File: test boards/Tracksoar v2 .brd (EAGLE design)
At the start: 50.4 x 19.6 mm, 53 parts, among them IC1 BME280, Y1 16MHZ

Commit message: added buck regulator
swapped the linear regulator for a buck converter.
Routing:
- net P$1: track 0.00 -> 9.58 mm, vias 0 -> 10
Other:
- board text added: "RX"
- board text added: "TX"
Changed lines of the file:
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@@
 <text x="-101.6" y="17.4752" size="0.6096" layer="25" rot="R270">3V</text>
 <text x="-99.695" y="17.4498" size="0.6096" layer="25" rot="R270">5V</text>
+<text x="-108.204" y="15.6718" size="0.8128" layer="25">RX</text>
+<text x="-108.077" y="17.8308" size="0.8128" layer="25">TX</text>
 </plain>
 <attributes>
@@
 <contactref element="C2" pad="1"/>
 <via x="-88.011" y="13.0048" extent="1-16" drill="0.5"/>
-<via x="-86.233" y="9.1186" extent="1-16" drill="0.5"/>
+<via x="-86.233" y="9.1186" extent="1-16" drill="0.6"/>
 <wire x1="-88.5444" y1="13.3604" x2="-88.1888" y2="13.0048" width="0.3048" layer="1"/>
 <wire x1="-88.1888" y1="13.0048" x2="-88.011" y2="13.0048" width="0.3048" layer="1"/>
@@
 <wire x1="-81.263" y1="11.2222" x2="-82.0212" y2="11.2222" width="0.3048" layer="16"/>
 <wire x1="-82.6262" y1="9.525" x2="-82.6516" y2="9.4996" width="0.3048" layer="16"/>
-<via x="-82.6516" y="9.4996" extent="1-16" drill="0.35"/>
+<via x="-82.6516" y="9.4996" extent="1-16" drill="0.6"/>
 <wire x1="-82.0212" y1="11.2222" x2="-82.6262" y2="10.6172" width="0.3048" layer="16"/>
 <wire x1="-82.6262" y1="10.6172" x2="-82.6262" y2="9.525" width="0.3048" layer="16"/>
@@
 <wire x1="-106.8832" y1="11.7498" x2="-107.5586" y2="11.7752" width="0.3048" layer="1"/>
 <wire x1="-107.5586" y1="11.7752" x2="-107.7824" y2="11.999" width="0.3048" layer="1"/>
-<via x="-108.7882" y="18.161" extent="1-16" drill="0.35" alwaysstop="yes"/>
+<via x="-108.7882" y="18.161" extent="1-16" drill="0.6" alwaysstop="yes"/>
 <wire x1="-111.6838" y1="18.1864" x2="-108.7882" y2="18.161" width="0.3048" layer="1"/>
 <wire x1="-112.5728" y1="17.2466" x2="-111.6838" y2="18.1864" width="0.3048" layer="1"/>
@@
 <wire x1="-109.6518" y1="17.4498" x2="-108.9152" y2="16.7132" width="0.3048" layer="1"/>
 <wire x1="-108.9152" y1="16.7132" x2="-108.9152" y2="16.129" width="0.3048" layer="1"/>
-<via x="-108.9152" y="16.129" extent="1-16" drill="0.35" alwaysstop="yes"/>
+<via x="-108.9152" y="16.129" extent="1-16" drill="0.6" alwaysstop="yes"/>
 <wire x1="-108.9152" y1="16.129" x2="-106.98" y2="14.1938" width="0.3048" layer="15"/>
 <wire x1="-104.729" y1="13.162" x2="-103.3018" y2="11.7348" width="0.3048" layer="15"/>
@@
 <wire x1="-106.98" y1="14.1938" x2="-105.23823125" y2="14.1938" width="0.3048" layer="15"/>
 <wire x1="-105.23823125" y1="14.1938" x2="-104.729" y2="13.68456875" width="0.3048" layer="15"/>
-<via x="-103.3018" y="11.7348" extent="1-16" drill="0.35"/>
+<via x="-103.3018" y="11.7348" extent="1-16" drill="0.6"/>
 <wire x1="-103.3018" y1="11.7348" x2="-103.3018" y2="11.1506" width="0.3048" layer="1"/>
 <wire x1="-103.3018" y1="11.1506" x2="-103.0732" y2="10.922" width="0.3048" layer="1"/>
@@
 <via x="-78.0034" y="4.064" extent="1-16" drill="1.183640625" diameter="1.6764" shape="square"/>
 </signal>
+<signal name="P$1">
+<via x="-79.2226" y="14.4018" extent="1-16" drill="0.35" alwaysstop="yes"/>
+<via x="-78.0034" y="14.4018" extent="1-16" drill="0.35" alwaysstop="yes"/>
+<via x="-78.5876" y="13.7922" extent="1-16" drill="0.35" alwaysstop="yes"/>
+<via x="-79.2226" y="13.1826" extent="1-16" drill="0.35" alwaysstop="yes"/>
+<via x="-78.0034" y="13.1826" extent="1-16" drill="0.35" alwaysstop="yes"/>
+<via x="-79.2226" y="11.8872" extent="1-16" drill="0.35" alwaysstop="yes"/>
+<via x="-78.0034" y="11.8618" extent="1-16" drill="0.35" alwaysstop="yes"/>
+<via x="-78.5876" y="11.2522" extent="1-16" drill="0.35" alwaysstop="yes"/>
+<via x="-79.2226" y="10.6426" extent="1-16" drill="0.35" alwaysstop="yes"/>
+<via x="-78.0034" y="10.6426" extent="1-16" drill="0.35" alwaysstop="yes"/>
+<wire x1="-79.2226" y1="14.4018" x2="-79.1972" y2="14.4018" width="0.1524" layer="16"/>
+<wire x1="-79.1972" y1="14.4018" x2="-78.5876" y2="13.7922" width="0.1524" layer="16"/>
+<wire x1="-78.5876" y1="13.7922" x2="-78.5876" y2="13.8176" width="0.1524" layer="16"/>
+<wire x1="-78.5876" y1="13.8176" x2="-78.0034" y2="14.4018" width="0.1524" layer="16"/>
+<wire x1="-78.0034" y1="13.1826" x2="-78.0034" y2="13.208" width="0.1524" layer="16"/>
+<wire x1="-78.0034" y1="13.208" x2="-78.5876" y2="13.7922" width="0.1524" layer="16"/>
+<wire x1="-78.5876" y1="13.7922" x2="-78.613" y2="13.7922" width="0.1524" layer="16"/>
+<wire x1="-78.613" y1="13.7922" x2="-79.2226" y2="13.1826" width="0.1524" layer="16"/>
+<wire x1="-79.2226" y1="11.8872" x2="-78.5876" y2="11.2522" width="0.1524" layer="16"/>
+<wire x1="-78.5876" y1="11.2522" x2="-78.5876" y2="11.2776" width="0.1524" layer="16"/>
+<wire x1="-78.5876" y1="11.2776" x2="-78.0034" y2="11.8618" width="0.1524" layer="16"/>
+<wire x1="-78.5876" y1="11.2522" x2="-78.5876" y2="11.2268" width="0.1524" layer="16"/>
+<wire x1="-78.5876" y1="11.2268" x2="-78.0034" y2="10.6426" width="0.1524" layer="16"/>
+<wire x1="-78.5876" y1="11.2522" x2="-78.613" y2="11.2522" width="0.1524" layer="16"/>
+<wire x1="-78.613" y1="11.2522" x2="-79.2226" y2="10.6426" width="0.1524" layer="16"/>
+<wire x1="-79.2226" y1="13.1826" x2="-79.2226" y2="11.8872" width="0.6096" layer="16"/>
+<wire x1="-78.0034" y1="11.8618" x2="-78.0034" y2="13.1826" width="0.6096" layer="16"/>
+</signal>
 </signals>

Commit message: fixed 3v reg
the 3v reg wiring was corrected and output cap moved closer to the regulator.
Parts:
- moved C15 7.38 mm to (-105.0, 13.0), turned to 0 degrees
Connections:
- removed net N$18: U$5.4, U$6.1
- new net N$21: U$5.5, U$6.2
- net 3V: now also U$5.4, U$6.1; no longer U$5.5, U$6.2
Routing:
- net VCC: track 45.2 -> 47.0 mm, vias 4 -> 3
- net N$21: track 0.00 -> 1.74 mm
- net GND: track 95.5 -> 97.0 mm
- net 3V: track 31.8 -> 30.9 mm
- removed copper zone on layer 16, net N$18
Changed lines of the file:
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@@
 <?xml version="1.0" encoding="utf-8"?>
 <!DOCTYPE eagle SYSTEM "eagle.dtd">
-<eagle version="8.7.0">
+<eagle version="8.6.3">
 <drawing>
 <settings>
@@
 <attribute name="VALUE" x="-100.0652" y="16.24" size="0.8128" layer="28" rot="MR270"/>
 </element>
-<element name="C15" library="SparkFun-Capacitors" library_urn="urn:adsk.eagle:library:510" package="0603" package3d_urn="urn:adsk.eagle:package:37414/1" value="10uF" x="-110.6424" y="17.7292" rot="MR270">
-<attribute name="PROD_ID" value="CAP-11015" x="-110.6424" y="17.7292" size="1.778" layer="28" rot="MR270" display="off"/>
+<element name="C15" library="SparkFun-Capacitors" library_urn="urn:adsk.eagle:library:510" package="0603" package3d_urn="urn:adsk.eagle:package:37414/1" value="10uF" x="-104.9528" y="13.0302" rot="MR0">
+<attribute name="PROD_ID" value="CAP-11015" x="-104.9528" y="13.0302" size="1.778" layer="28" rot="MR0" display="off"/>
 </element>
 <element name="C16" library="SparkFun-Capacitors" library_urn="urn:adsk.eagle:library:510" package="0603" package3d_urn="urn:adsk.eagle:package:37414/1" value="10uF" x="-107.5436" y="15.9512" smashed="yes" rot="MR270">
@@
 <contactref element="C16" pad="2"/>
 <wire x1="-109.1438" y1="14.771" x2="-109.1438" y2="14.5796" width="0.3048" layer="16"/>
-<via x="-106.9594" y="13.4112" extent="1-16" drill="0.6"/>
+<via x="-107.1626" y="13.6144" extent="1-16" drill="0.6"/>
 <wire x1="-107.5436" y1="15.1012" x2="-107.5436" y2="13.9954" width="0.6096" layer="16"/>
-<wire x1="-107.5436" y1="13.9954" x2="-106.9594" y2="13.4112" width="0.6096" layer="16"/>
-<wire x1="-106.9636" y1="13.4366" x2="-106.9594" y2="13.4112" width="0.6096" layer="1"/>
+<wire x1="-107.5436" y1="13.9954" x2="-107.1626" y2="13.6144" width="0.6096" layer="16"/>
+<wire x1="-106.9636" y1="13.4366" x2="-107.1626" y2="13.6144" width="0.6096" layer="1"/>
 <wire x1="-106.0904" y1="15.4686" x2="-106.846" y2="15.4686" width="0.6096" layer="16"/>
 <wire x1="-106.846" y1="15.4686" x2="-107.5436" y2="15.1012" width="0.6096" layer="16"/>
@@
 <wire x1="-79.8068" y1="16.6116" x2="-80.6704" y2="17.4752" width="0.6096" layer="16"/>
 <wire x1="-80.6704" y1="17.4752" x2="-80.6704" y2="17.8054" width="0.6096" layer="16"/>
+<wire x1="-105.8028" y1="13.0302" x2="-106.5784" y2="13.0302" width="0.6096" layer="16"/>
+<wire x1="-106.5784" y1="13.0302" x2="-107.1626" y2="13.6144" width="0.6096" layer="16"/>
 </signal>
 <signal name="VCC">
@@
 <vertex x="-105.6386" y="16.2306"/>
 </polygon>
-<via x="-105.5116" y="13.3604" extent="1-16" drill="0.6"/>
-<wire x1="-106.0904" y1="14.5186" x2="-106.0904" y2="13.9138" width="0.6096" layer="16"/>
-<wire x1="-106.0904" y1="13.9138" x2="-105.8926" y2="13.716" width="0.6096" layer="16"/>
-<wire x1="-105.8926" y1="13.716" x2="-105.5116" y2="13.3604" width="0.6096" layer="16"/>
 <via x="-106.045" y="17.4244" extent="1-16" drill="0.6"/>
 <via x="-94.5642" y="4.1402" extent="1-16" drill="0.6"/>
@@
 <wire x1="-88.9762" y1="9.3726" x2="-88.5952" y2="9.3726" width="0.3048" layer="1"/>
 <wire x1="-88.5952" y1="9.3726" x2="-88.116321875" y2="8.893721875" width="0.3048" layer="1"/>
+<wire x1="-106.0904" y1="14.5186" x2="-105.4964" y2="14.5186" width="0.2032" layer="16"/>
+<wire x1="-105.4964" y1="14.5186" x2="-105.283" y2="14.732" width="0.2032" layer="16"/>
+<wire x1="-105.283" y1="14.732" x2="-105.283" y2="16.1798" width="0.2032" layer="16"/>
+<wire x1="-105.283" y1="16.1798" x2="-105.537" y2="16.4338" width="0.2032" layer="16"/>
+<wire x1="-105.537" y1="16.4338" x2="-105.5522" y2="16.4186" width="0.2032" layer="16"/>
+<wire x1="-105.5522" y1="16.4186" x2="-106.0904" y2="16.4186" width="0.2032" layer="16"/>
 </signal>
 <signal name="D3">
@@
 <wire x1="-118.0846" y1="17.3228" x2="-118.0846" y2="15.7716" width="0.6096" layer="1"/>
 <wire x1="-118.0846" y1="15.7716" x2="-118.0834" y2="15.7704" width="0.3048" layer="1"/>
-<wire x1="-101.2444" y1="16.535396875" x2="-101.2698" y2="18.0998" width="0.4064" layer="1"/>
+<wire x1="-101.2698" y1="16.535396875" x2="-101.2698" y2="18.0998" width="0.4064" layer="1"/>
 <wire x1="-101.2698" y1="18.0998" x2="-101.2086" y2="18.3642" width="0.3048" layer="1"/>
-<wire x1="-101.2444" y1="16.535396875" x2="-102.64381875" y2="15.16621875" width="0.4064" layer="1"/>
+<wire x1="-101.2698" y1="16.535396875" x2="-102.64381875" y2="15.16621875" width="0.4064" layer="1"/>
 <contactref element="C11" pad="2"/>
 <contactref element="C14" pad="2"/>
@@
 <wire x1="-106.3752" y1="7.2136" x2="-106.3752" y2="6.8834" width="0.3048" layer="16"/>
 <wire x1="-106.3752" y1="6.8834" x2="-105.844221875" y2="6.37781875" width="0.3048" layer="16"/>
-<contactref element="U$5" pad="5"/>
-<contactref element="U$6" pad="2"/>
 <contactref element="C15" pad="1"/>
 <wire x1="-114.2144" y1="18.376" x2="-114.3254" y2="18.487" width="0.3048" layer="16"/>
 <wire x1="-118.1438" y1="18.487" x2="-118.165" y2="18.4658" width="0.3048" layer="16"/>
-<polygon width="0.3048" layer="16" thermals="no">
-<vertex x="-101.2444" y="14.8336"/>
-<vertex x="-104.14" y="14.8336"/>
-<vertex x="-104.14" y="13.6144"/>
-<vertex x="-101.2444" y="13.6144"/>
-</polygon>
 <polygon width="0.3048" layer="16" isolate="0.3048" thermals="no" rank="3">
 <vertex x="-100.5078" y="19.304"/>
@@
 <vertex x="-117.348" y="16.8402"/>
 <vertex x="-117.348" y="17.9832"/>
-<vertex x="-102.1588" y="17.9832"/>
-<vertex x="-102.1588" y="17.6784"/>
+<vertex x="-104.8004" y="17.9832"/>
+<vertex x="-104.8004" y="15.6718"/>
+<vertex x="-101.1682" y="15.6718"/>
+<vertex x="-101.1174" y="17.6784"/>
 <vertex x="-100.5078" y="17.6784"/>
 </polygon>
 <wire x1="-105.152278125" y1="9.554121875" x2="-104.212475" y2="10.504525" width="0.6096" layer="16"/>
-<wire x1="-104.212475" y1="10.504525" x2="-104.1908" y2="13.843" width="0.6096" layer="16"/>
-<wire x1="-104.1908" y1="13.843" x2="-103.5152" y2="14.5186" width="0.6096" layer="16"/>
-<wire x1="-103.5152" y1="14.5186" x2="-103.5004" y2="14.5186" width="0.6096" layer="16"/>
-<wire x1="-103.5004" y1="14.5186" x2="-104.3076" y2="14.5186" width="0.6096" layer="16"/>
-<wire x1="-104.3076" y1="14.5186" x2="-104.8512" y2="15.0622" width="0.6096" layer="16"/>
-<wire x1="-104.8512" y1="15.0622" x2="-104.8512" y2="18.0848" width="0.6096" layer="16"/>
 <wire x1="-104.8512" y1="18.0848" x2="-104.5718" y2="18.3642" width="0.6096" layer="16"/>
 <wire x1="-104.5718" y1="18.3642" x2="-101.2086" y2="18.3642" width="0.6096" layer="16"/>
+<contactref element="U$5" pad="4"/>
+<contactref element="U$6" pad="1"/>
+<wire x1="-101.8818" y1="16.4186" x2="-101.854" y2="16.3908" width="0.1524" layer="16"/>
+<wire x1="-101.854" y1="17.7188" x2="-101.2086" y2="18.3642" width="0.1524" layer="16"/>
+<wire x1="-104.212475" y1="10.504525" x2="-104.212475" y2="12.874075" width="0.6096" layer="16"/>
+<wire x1="-104.212475" y1="12.874075" x2="-104.648" y2="13.335" width="0.6096" layer="16"/>
+<wire x1="-104.648" y1="13.335" x2="-104.648" y2="15.6972" width="0.6096" layer="16"/>
+<wire x1="-104.648" y1="15.6972" x2="-104.0384" y2="16.4338" width="0.6096" layer="16"/>
+<wire x1="-104.0384" y1="16.4338" x2="-104.0232" y2="16.4186" width="0.6096" layer="16"/>
+<wire x1="-104.0232" y1="16.4186" x2="-103.5004" y2="16.4186" width="0.6096" layer="16"/>
+<wire x1="-104.1028" y1="13.0302" x2="-104.1028" y2="12.98375" width="0.6096" layer="16"/>
+<wire x1="-104.1028" y1="12.98375" x2="-104.212475" y2="12.874075" width="0.6096" layer="16"/>
 </signal>
 <signal name="N$1">
@@
 <wire x1="-107.5586" y1="11.7752" x2="-107.7824" y2="11.999" width="0.3048" layer="1"/>
 <via x="-108.7882" y="18.161" extent="1-16" drill="0.6" alwaysstop="yes"/>
-<wire x1="-111.6838" y1="18.1864" x2="-108.7882" y2="18.161" width="0.3048" layer="1"/>
-<wire x1="-112.5728" y1="17.2466" x2="-111.6838" y2="18.1864" width="0.3048" layer="1"/>
+<wire x1="-111.6838" y1="18.161" x2="-108.7882" y2="18.161" width="0.3048" layer="1"/>
+<wire x1="-112.5728" y1="17.2466" x2="-111.6838" y2="18.161" width="0.3048" layer="1"/>
 <wire x1="-108.7882" y1="18.161" x2="-108.077" y2="17.5006" width="0.3048" layer="1"/>
 <wire x1="-108.077" y1="17.5006" x2="-108.077" y2="12.2682" width="0.3048" layer="1"/>
@@
 <wire x1="-93.24814375" y1="6.53254375" x2="-93.248140625" y2="6.540728125" width="0.3048" layer="1"/>
 </signal>
-<signal name="N$18">
-<contactref element="U$6" pad="1"/>
-<contactref element="U$5" pad="4"/>
-<polygon width="0.3048" layer="16" thermals="no">
-<vertex x="-101.219" y="16.9672"/>
-<vertex x="-101.219" y="15.6464"/>
-<vertex x="-104.14" y="15.6464"/>
-<vertex x="-104.14" y="16.9672"/>
-</polygon>
-</signal>
 <signal name="RX1">
 <contactref element="U$1" pad="2_TXD1"/>
@@
 <wire x1="-78.0034" y1="11.8618" x2="-78.0034" y2="13.1826" width="0.6096" layer="16"/>
 </signal>
+<signal name="N$21">
+<contactref element="U$5" pad="5"/>
+<contactref element="U$6" pad="2"/>
+<wire x1="-103.5004" y1="14.5186" x2="-102.0818" y2="14.5186" width="0.7112" layer="16"/>
+<wire x1="-102.0818" y1="14.5186" x2="-101.854" y2="14.2908" width="0.6096" layer="16"/>
+</signal>
 </signals>

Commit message: Added gps backup cap
added gps backup capacitor. Corrected serial voltage divider resistor values. Removed ground vias below gps module.
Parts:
- added C17: .1uf, SparkFun-Capacitors:0402-CAP
- added C3: DSK-3R3H204T614-H2L, DSK-3R3H204T614-H2L:DSK-3R3H204T614-H2L
- added D2: (no value), adafruit:SOD-123
- added R17: 330, adafruit:R0402
- R14: value 4.7k -> 10k
- R15: value 10k -> 4.7k
- moved C11 3.89 mm to (-110.4, 17.8)
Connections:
- new net N$22: D2.C, R17.1
- new net VBACKUP: C17.2, C3.1, R17.2, U$1.6_V_BCKP
- net 3V: now also D2.A; no longer U$1.6_V_BCKP
- net GND: now also C17.1, C3.2
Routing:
- net VBACKUP: track 0.00 -> 13.8 mm, vias 0 -> 1
- net 3V: track 30.9 -> 38.0 mm
- net N$22: track 0.00 -> 1.79 mm
- net GND: track 97.0 -> 96.8 mm, vias 82 -> 30

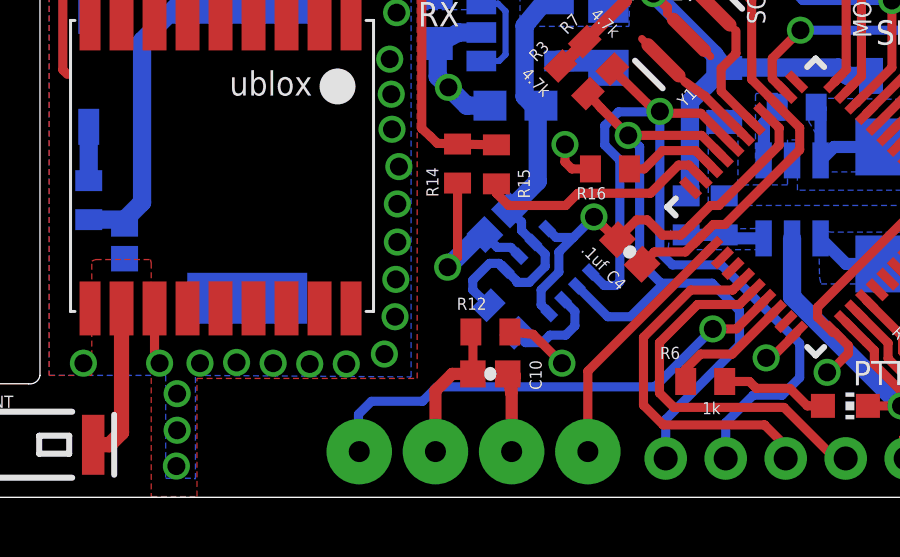
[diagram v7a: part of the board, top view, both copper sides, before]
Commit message: minor trace cleanup
moved a few traces around for aesthetics.
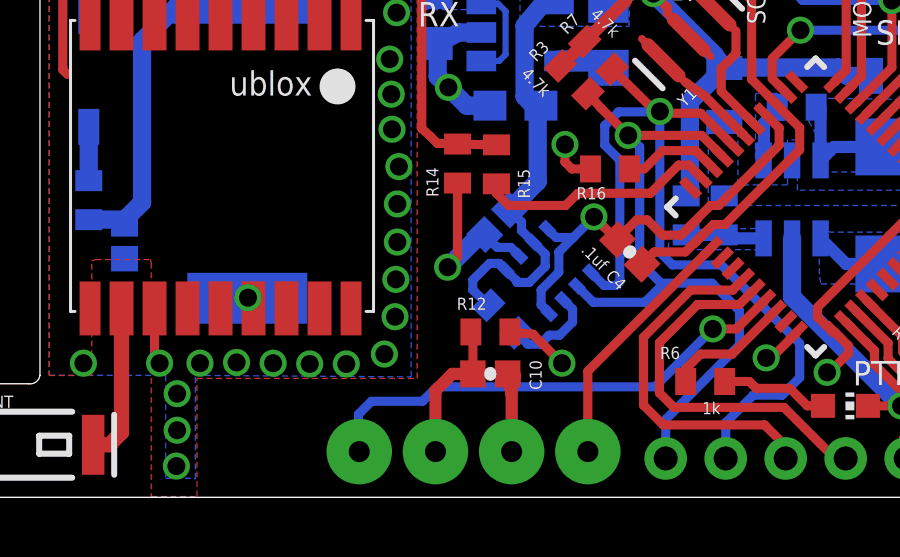
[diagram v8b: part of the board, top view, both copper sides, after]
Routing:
- net GND: vias 30 -> 31
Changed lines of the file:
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@@
 <?xml version="1.0" encoding="utf-8"?>
 <!DOCTYPE eagle SYSTEM "eagle.dtd">
-<eagle version="8.6.3">
+<eagle version="8.7.1">
 <drawing>
 <settings>
@@
 <contactref element="C3" pad="2"/>
 <contactref element="C17" pad="1"/>
+<via x="-113.8682" y="6.6294" extent="1-16" drill="0.6"/>
 </signal>
 <signal name="VCC">
@@
 <contactref element="U$3" pad="6"/>
 <wire x1="-99.9452" y1="2.5692" x2="-99.9452" y2="1.27" width="0.3048" layer="16"/>
-<wire x1="-102.90600625" y1="7.023425" x2="-101.876978125" y2="5.9944" width="0.3048" layer="16"/>
-<wire x1="-101.876978125" y1="5.9944" x2="-101.1174" y2="5.9944" width="0.3048" layer="16"/>
-<wire x1="-101.1174" y1="5.9944" x2="-100.1014" y2="7.0104" width="0.3048" layer="16"/>
 <wire x1="-100.1014" y1="7.0104" x2="-100.1014" y2="7.112" width="0.3048" layer="16"/>
+<wire x1="-102.90600625" y1="7.023425" x2="-102.35958125" y2="6.477" width="0.3048" layer="16"/>
+<wire x1="-100.6348" y1="6.477" x2="-100.1014" y2="7.0104" width="0.3048" layer="16"/>
+<wire x1="-102.35958125" y1="6.477" x2="-100.6348" y2="6.477" width="0.3048" layer="16"/>
 </signal>
 <signal name="SCL">
@@
 <contactref element="IC1" pad="2"/>
 <contactref element="R2" pad="2"/>
-<wire x1="-103.365628125" y1="6.563803125" x2="-102.9716" y2="6.169778125" width="0.3048" layer="16"/>
-<wire x1="-102.9716" y1="6.169778125" x2="-102.9716" y2="5.6896" width="0.3048" layer="16"/>
-<wire x1="-102.9716" y1="5.6896" x2="-103.2812" y2="5.38" width="0.3048" layer="16"/>
-<wire x1="-103.2812" y1="5.38" x2="-103.80376875" y2="5.38" width="0.3048" layer="16"/>
-<wire x1="-103.80376875" y1="5.38" x2="-104.05296875" y2="5.1308" width="0.3048" layer="16"/>
-<wire x1="-104.6226" y1="5.1308" x2="-104.92498125" y2="5.458578125" width="0.3048" layer="16"/>
-<wire x1="-104.05296875" y1="5.1308" x2="-104.6226" y2="5.1308" width="0.3048" layer="16"/>
+<wire x1="-103.365628125" y1="6.563803125" x2="-103.0478" y2="6.245978125" width="0.3048" layer="16"/>
+<wire x1="-103.0478" y1="6.245978125" x2="-103.0478" y2="5.8166" width="0.3048" layer="16"/>
+<wire x1="-103.0478" y1="5.8166" x2="-103.4844" y2="5.38" width="0.3048" layer="16"/>
+<wire x1="-103.4844" y1="5.38" x2="-103.82916875" y2="5.38" width="0.3048" layer="16"/>
+<wire x1="-103.82916875" y1="5.38" x2="-104.12916875" y2="5.08" width="0.3048" layer="16"/>
+<wire x1="-104.5464" y1="5.08" x2="-104.92498125" y2="5.458578125" width="0.3048" layer="16"/>
+<wire x1="-104.12916875" y1="5.08" x2="-104.5464" y2="5.08" width="0.3048" layer="16"/>
 </signal>
 <signal name="N$7">
